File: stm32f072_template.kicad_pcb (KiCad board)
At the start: 2 copper layers, 20.3 x 50.8 mm, 23 parts, among them J1 USB_C_Receptacle_USB2.0, J2 Conn_01x20, J3 Conn_01x20, U1 STM32F072CBT6, U2 PRTR5V0U2X, U3 XC6206PxxxMR-Regulator_Linear

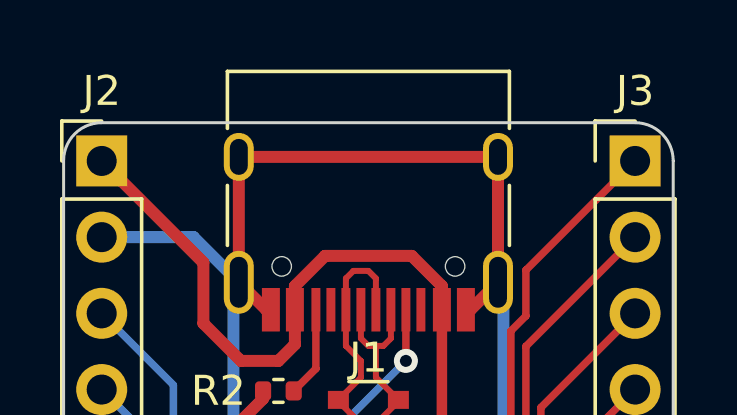
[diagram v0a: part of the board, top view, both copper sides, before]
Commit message: replace USB footprint
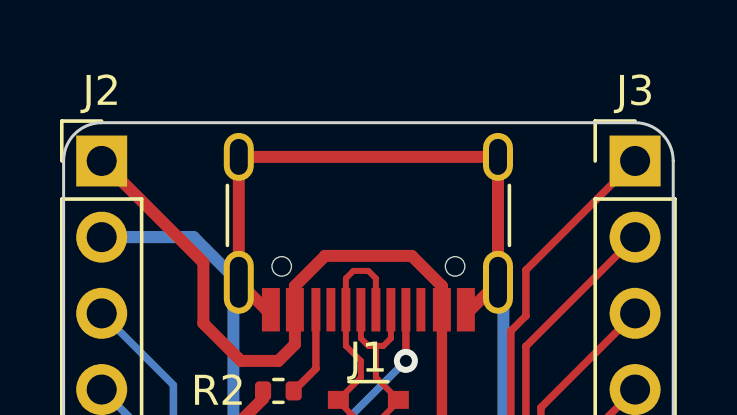
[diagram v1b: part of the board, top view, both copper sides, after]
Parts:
- J1: footprint Connector_USB:USB_C_Receptacle_HRO_TYPE-C-31-M-12 -> PCM_marbastlib-various:USB_C_Receptacle_HRO_TYPE-C-31-M-12
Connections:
- U2 pad 2: D_N -> D-
- U2 pad 3: D_P -> D+
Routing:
- net D_P: track 22.1 -> 0.00 mm
- net D+: track 0.00 -> 22.1 mm
- net D_N: track 20.5 -> 0.00 mm
- net D-: track 0.00 -> 20.5 mm
